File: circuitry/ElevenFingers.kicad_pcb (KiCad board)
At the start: 2 copper layers, 5.1 x 5.1 mm, 95 parts, among them J1 OLED, SW1 MX, SW10 MX, SW11 MX, SW12 MX, SW13 MX, SW14 MX, SW15 MX, SW16 MX, SW17 MX, SW18 MX, SW19 MX, SW2 MX, SW20 MX, SW21 MX, SW22 MX, SW23 MX, SW24 MX, SW25 MX, SW26 MX, SW27 MX, SW28 MX, SW29 MX, SW3 MX, SW30 MX, SW4 MX, SW5 MX, SW6 MX, SW7 MX, SW8 MX, SW9 MX, U1 ProMicro, U2 TRRS

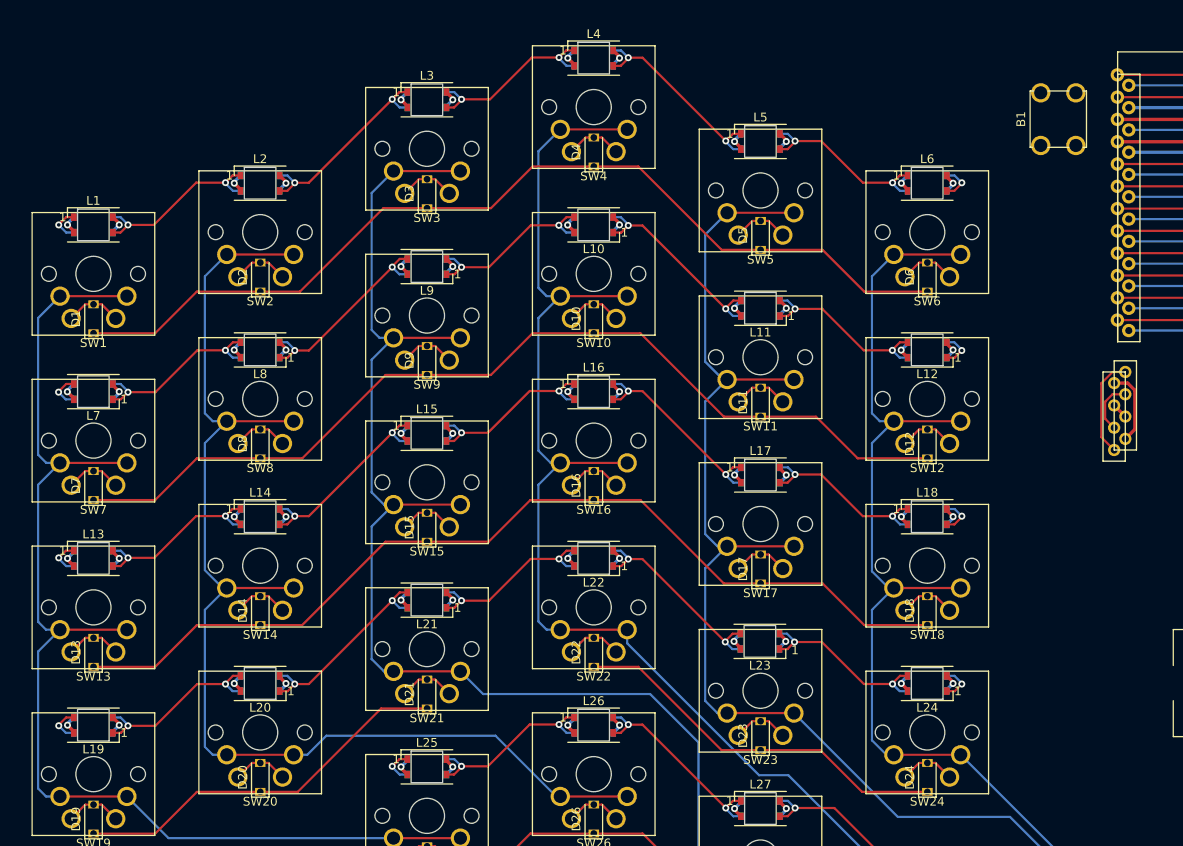
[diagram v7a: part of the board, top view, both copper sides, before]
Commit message: routed rows and cols to ProMicro
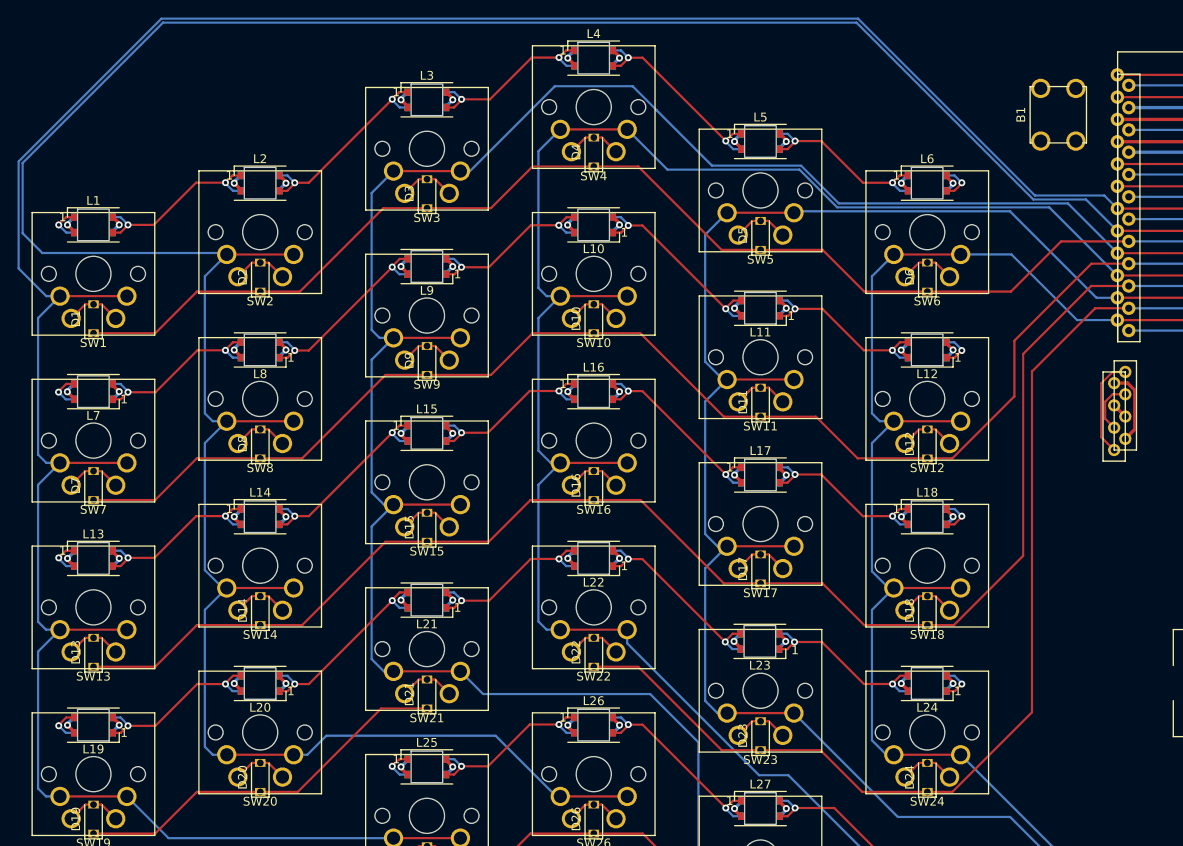
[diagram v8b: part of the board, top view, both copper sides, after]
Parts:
- moved B1 0.50 mm to (148.0, 61.2)
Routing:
- net col1: track 154.6 -> 328.1 mm
- net col0: track 153.5 -> 312.6 mm
- net col2: track 168.3 -> 255.1 mm
- net row3: track 102.2 -> 170.8 mm
- net col3: track 173.2 -> 235.9 mm
- net row2: track 123.2 -> 175.6 mm
- net col4: track 179.6 -> 220.6 mm
- net row1: track 123.2 -> 159.1 mm
- net row0: track 123.2 -> 148.5 mm
- net col5: track 183.7 -> 204.7 mm
